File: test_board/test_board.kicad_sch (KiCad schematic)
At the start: 14 parts, among them J1 Conn_01x24_Socket, J2 Conn_01x24_Socket, SW1 CJS-1201B, U14 REF3012, U15 REF3025, U4 HT7533-1_C14289

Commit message: added uart connector
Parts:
- added J3: Conn_01x02_Pin, Connector_PinHeader_2.54mm:PinHeader_1x02_P2.54mm_Vertical, symbol Connector:Conn_01x02_Pin
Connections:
- net pin22: now reaches J1.22 (Pin_22)
- net pin22: now also J3.1 (Pin_1)
- net pin23: now reaches J1.23 (Pin_23)
- net pin23: now also J3.2 (Pin_2)
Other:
- note added: "5V current budget: Per datasheet FPGA worst case power consumption: 1.2A @ 1V 0.6A @ 1.8V 0.6A @ 3.3V 4.26 W total 0.0625 @ 5V from comparators 4.57 W 915 mA, USB 3.0 ports max out at 900mA, 2.0 maxes out at 500mA If we have problems we use an external 5V/2A USB supply then communicate to pc over a broken out UART interface"
- note added: "Extra pins broken out in case we need an additional comms interface"
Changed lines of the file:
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@@
 		)
 	)
+	(text "5V current budget:\nPer datasheet FPGA worst case power consumption:\n1.2A @ 1V \n0.6A @ 1.8V\n0.6A @ 3.3V\n4.26 W total\n0.0625 @ 5V from comparators\n4.57 W\n915 mA, USB 3.0 ports max out at 900mA, 2.0 maxes out at 500mA\nIf we have problems we use an external 5V/2A USB supply\nthen communicate to pc over a broken out UART interface"
+		(exclude_from_sim no)
+		(at 15.24 173.355 0)
+		(effects
+			(font
+				(size 1.27 1.27)
+			)
+			(justify left)
+		)
+	)
 	(text "3.3V current budget:\nComparators: 5.8 mA * 10 = 58 mA\nVoltage reference dividers: 700uA * 10 = 7mA\nVoltage reference quiescent: 25uA * 10 = 250uA\nTotal: 65.25 mA"
 		(exclude_from_sim no)
-		(at 26.67 152.4 0)
+		(at 15.24 153.035 0)
+		(effects
+			(font
+				(size 1.27 1.27)
+			)
+			(justify left)
+		)
+	)
+	(text "Extra pins broken out in case we\nneed an additional comms interface"
+		(exclude_from_sim no)
+		(at 42.545 191.135 0)
 		(effects
 			(font
@@
 		)
 	)
+	(global_label "pin22"
+		(shape bidirectional)
+		(at 95.25 170.18 180)
+		(fields_autoplaced yes)
+		(effects
+			(font
+				(size 1.27 1.27)
+			)
+			(justify right)
+		)
+		(property "Intersheetrefs" "${INTERSHEET_REFS}"
+			(at 85.8317 170.18 0)
+			(effects
+				(font
+					(size 1.27 1.27)
+				)
+				(justify right)
+				(hide yes)
+			)
+		)
+	)
+	(global_label "pin23"
+		(shape bidirectional)
+		(at 90.17 192.405 0)
+		(fields_autoplaced yes)
+		(effects
+			(font
+				(size 1.27 1.27)
+			)
+			(justify left)
+		)
+		(property "Intersheetrefs" "${INTERSHEET_REFS}"
+			(at 99.5883 192.405 0)
+			(effects
+				(font
+					(size 1.27 1.27)
+				)
+				(justify left)
+				(hide yes)
+			)
+		)
+	)
 	(global_label "out2"
 		(shape input)
@@
 		)
 	)
+	(global_label "pin23"
+		(shape bidirectional)
+		(at 95.25 172.72 180)
+		(fields_autoplaced yes)
+		(effects
+			(font
+				(size 1.27 1.27)
+			)
+			(justify right)
+		)
+		(property "Intersheetrefs" "${INTERSHEET_REFS}"
+			(at 85.8317 172.72 0)
+			(effects
+				(font
+					(size 1.27 1.27)
+				)
+				(justify right)
+				(hide yes)
+			)
+		)
+	)
+	(global_label "pin22"
+		(shape bidirectional)
+		(at 90.17 189.865 0)
+		(fields_autoplaced yes)
+		(effects
+			(font
+				(size 1.27 1.27)
+			)
+			(justify left)
+		)
+		(property "Intersheetrefs" "${INTERSHEET_REFS}"
+			(at 99.5883 189.865 0)
+			(effects
+				(font
+					(size 1.27 1.27)
+				)
+				(justify left)
+				(hide yes)
+			)
+		)
+	)
 	(global_label "vref"
 		(shape input)
@@
 					(unit 1)
 				)
+			)
+		)
+	)
+	(symbol
+		(lib_id "Connector:Conn_01x02_Pin")
+		(at 85.09 189.865 0)
+		(unit 1)
+		(exclude_from_sim no)
+		(in_bom yes)
+		(on_board yes)
+		(dnp yes)
+		(fields_autoplaced yes)
+		(property "Reference" "J3"
+			(at 85.725 184.785 0)
+			(effects
+				(font
+					(size 1.27 1.27)
+				)
+			)
+		)
+		(property "Value" "Conn_01x02_Pin"
+			(at 85.725 187.325 0)
+			(effects
+				(font
+					(size 1.27 1.27)
+				)
+			)
+		)
+		(property "Footprint" "Connector_PinHeader_2.54mm:PinHeader_1x02_P2.54mm_Vertical"
+			(at 85.09 189.865 0)
+			(effects
+				(font
+					(size 1.27 1.27)
+				)
+				(hide yes)
+			)
+		)
+		(property "Datasheet" "~"
+			(at 85.09 189.865 0)
+			(effects
+				(font
+					(size 1.27 1.27)
+				)
+				(hide yes)
+			)
+		)
+		(property "Description" "Generic connector, single row, 01x02, script generated"
+			(at 85.09 189.865 0)
+			(effects
+				(font
+					(size 1.27 1.27)
+				)
+				(hide yes)
+			)
+		)
+		(pin "1"
+		)
+		(pin "2"
+		)
+		(instances
+			(project ""
+				(path "/f01d8a8e-7bb6-4363-8f3a-aad691292558"
+					(reference "J3")
+					(unit 1)
+				)

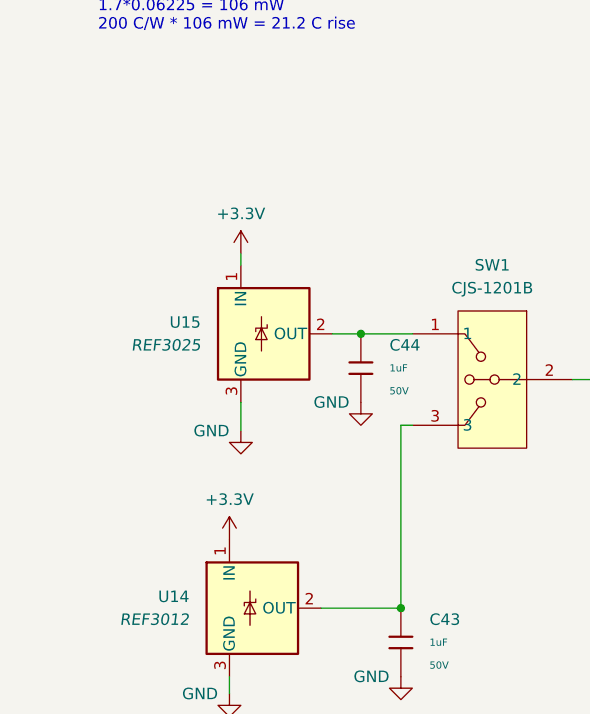
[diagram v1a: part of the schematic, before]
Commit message: added decoupling caps to regulator and changed comparator termination resistor to 49.9 ohm
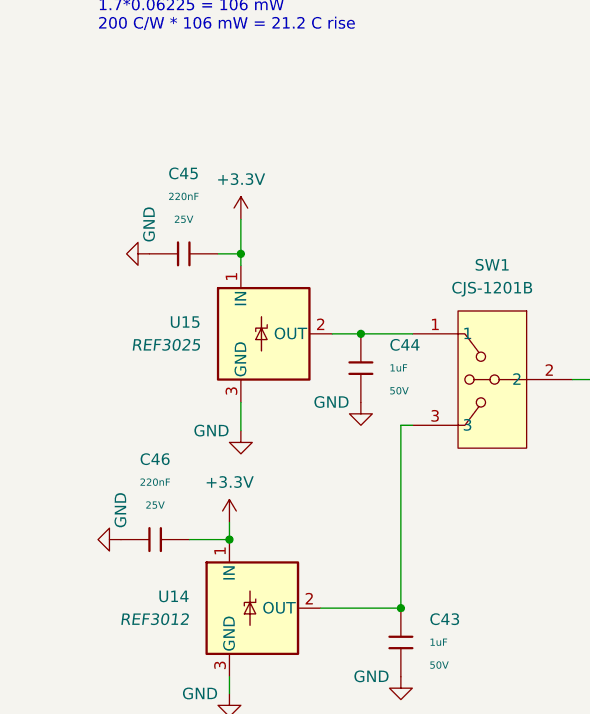
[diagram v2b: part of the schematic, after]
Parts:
- added C45, C46: 220nF, PCM_JLCPCB:C_0603, symbol PCM_JLCPCB-Capacitors:0603,220nF
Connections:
- net +3.3V: now also C45.2, C46.2
- net GND: now also C45.1, C46.1

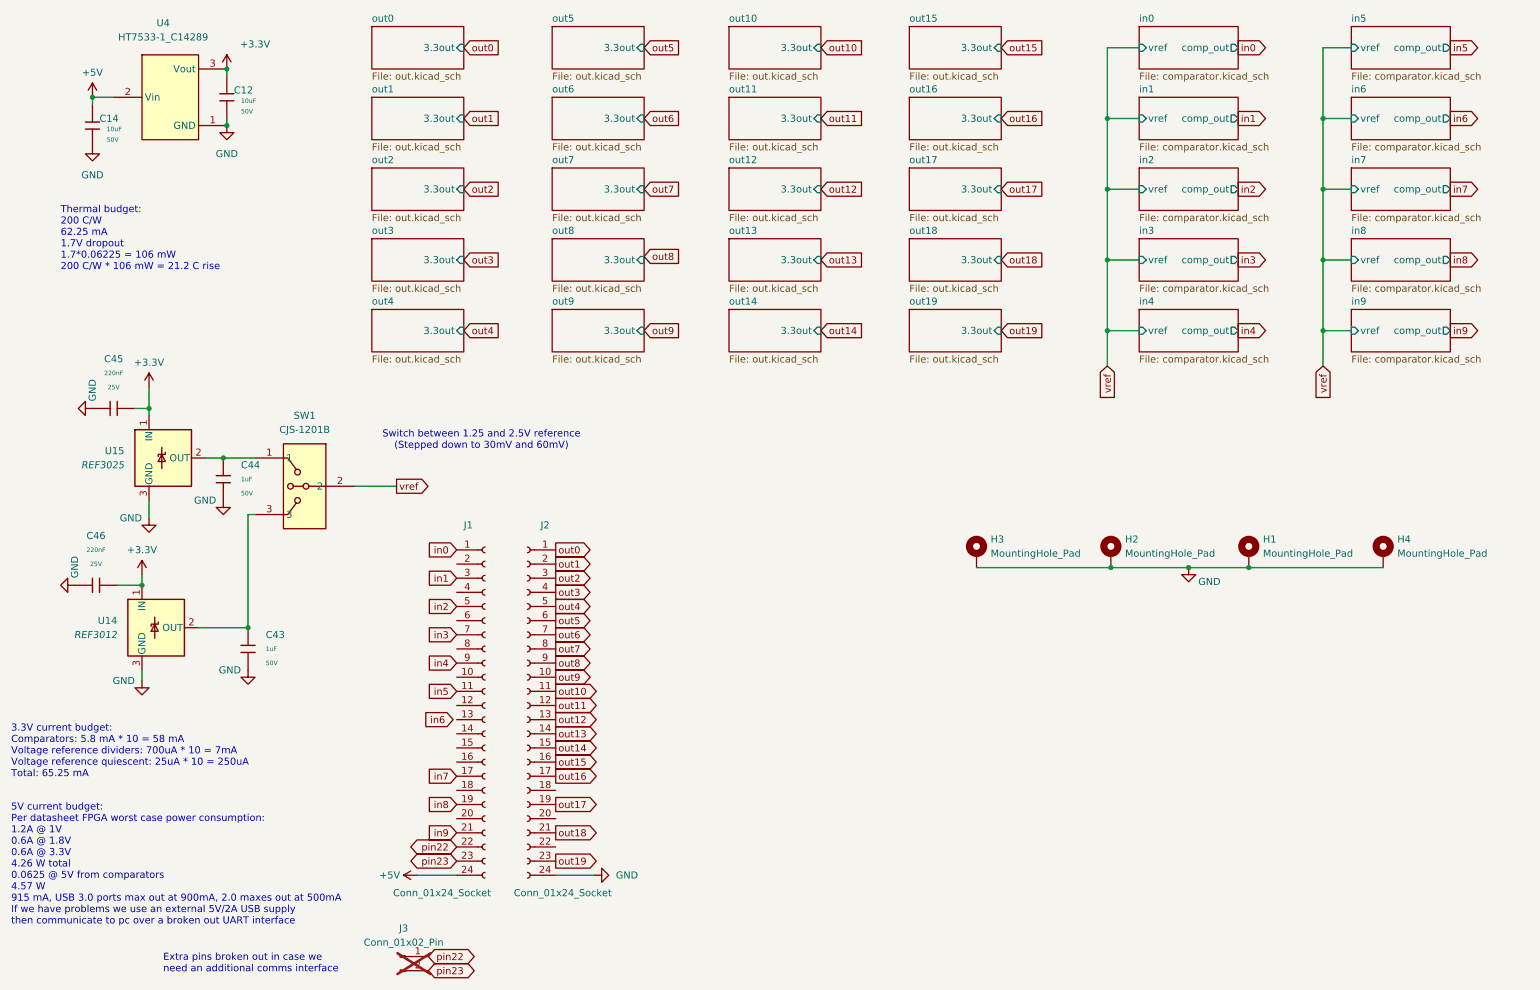
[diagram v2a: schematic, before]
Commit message: spaced out SMA connectors
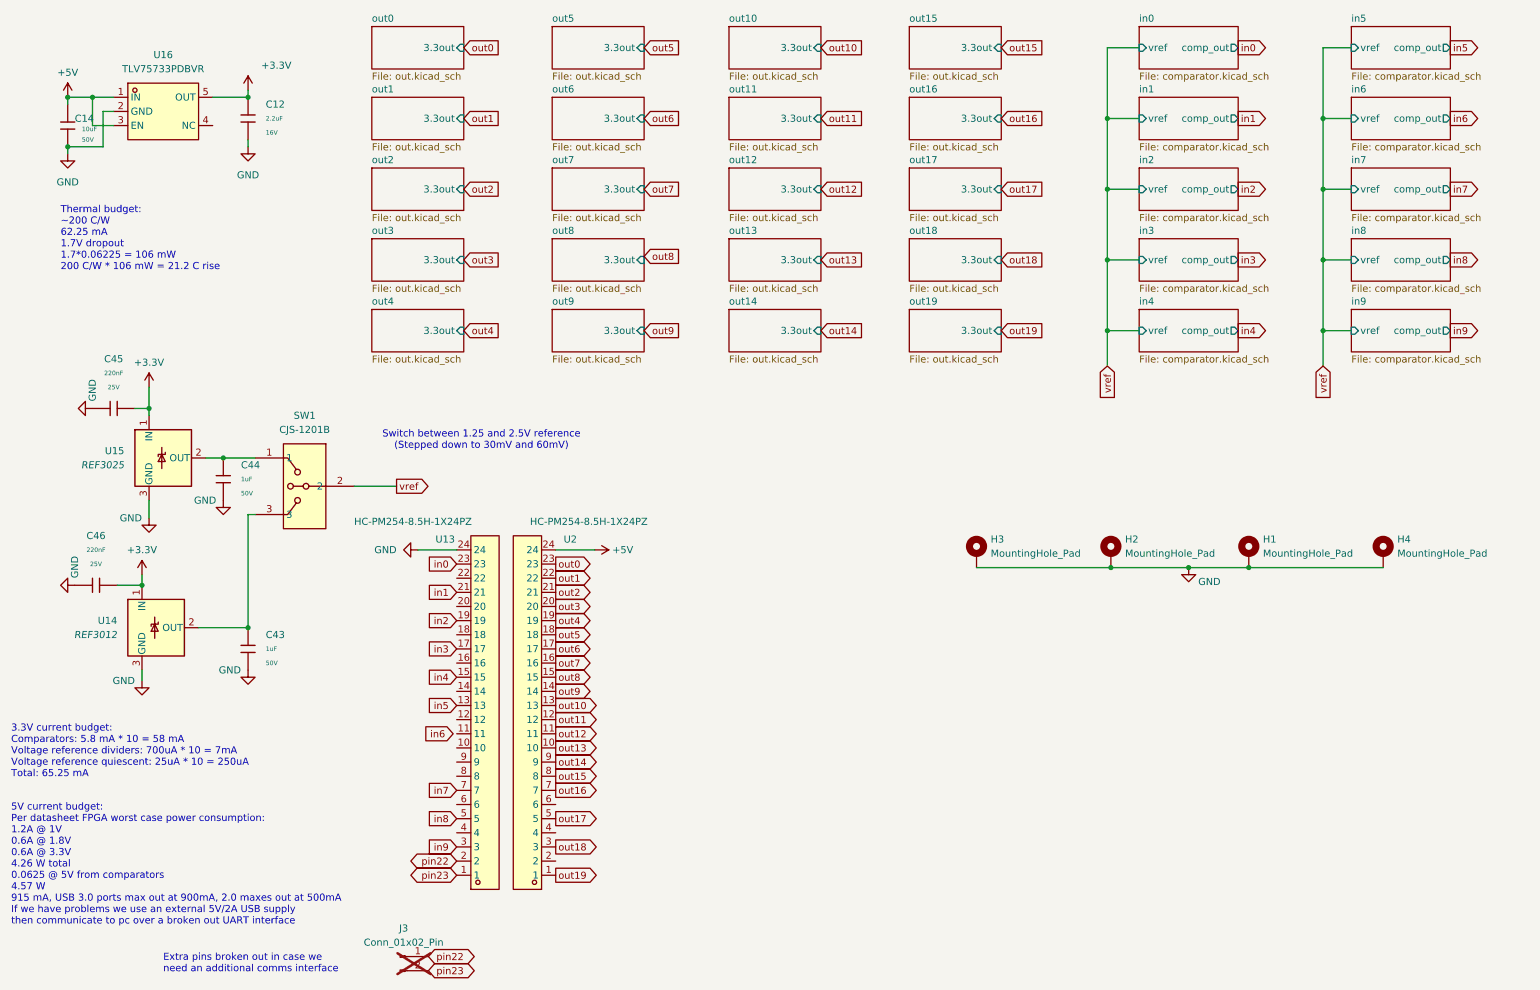
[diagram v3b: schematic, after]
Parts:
- removed C12: 10uF, PCM_JLCPCB:C_0805, symbol PCM_JLCPCB-Capacitors:0805,10uF,(2)
- removed J1, J2: Conn_01x24_Socket, Connector_PinSocket_2.54mm:PinSocket_1x24_P2.54mm_Vertical, symbol Connector:Conn_01x24_Socket
- removed U4: HT7533-1_C14289, easyeda2kicad:SOT-89-3_L4.5-W2.5-P1.50-LS4.2-BR, symbol easyeda2kicad:HT7533-1_C14289
- added C12: 2.2uF, PCM_JLCPCB:C_0603, symbol PCM_JLCPCB-Capacitors:0603,2.2uF
- added U13, U2: HC-PM254-8.5H-1X24PZ, easyeda2kicad:HDR-TH_24P-P2.54-V-F, symbol easyeda2kicad:HC-PM254-8.5H-1X24PZ
- added U16: TLV75733PDBVR, easyeda2kicad:SOT-23-5_L2.9-W1.6-P0.95-LS2.8-BL, symbol easyeda2kicad:TLV75733PDBVR
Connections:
- net +3.3V: now also C12.1, U16.5 (OUT)
- net +5V: now also U16.1 (IN), U16.3 (EN), U2.24
- net GND: now also C12.2, U13.24, U16.2 (GND)
- net in0: now also U13.23
- net in1: now also U13.21
- net in2: now also U13.19
- net in3: now also U13.17
- net in4: now also U13.15
- net in5: now also U13.13
- net in7: now also U13.7
- net in8: now also U13.5
- net in9: now also U13.3
- net out0: now also U2.23
- net out1: now also U2.22
- net out10: now also U2.13
- net out11: now also U2.12
- net out12: now also U2.11
- net out13: now also U2.10
- net out14: now also U2.9
- net out15: now also U2.8
- net out16: now also U2.7
- net out17: now also U2.5
- net out18: now also U2.3
- net out19: now also U2.1
- net out2: now also U2.21
- net out3: now also U2.20
- net out4: now also U2.19
- net out5: now also U2.18
- net out6: now also U2.17
- net out7: now also U2.16
- net out8: now also U2.15
- net out9: now also U2.14
- net pin22: now also U13.2
- net pin23: now also U13.1
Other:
- note added: "Thermal budget: ~200 C/W 62.25 mA 1.7V dropout 1.7*0.06225 = 106 mW 200 C/W * 106 mW = 21.2 C rise"
- note removed: "Thermal budget: 200 C/W 62.25 mA 1.7V dropout 1.7*0.06225 = 106 mW 200 C/W * 106 mW = 21.2 C rise"
- moved on the sheet: C14

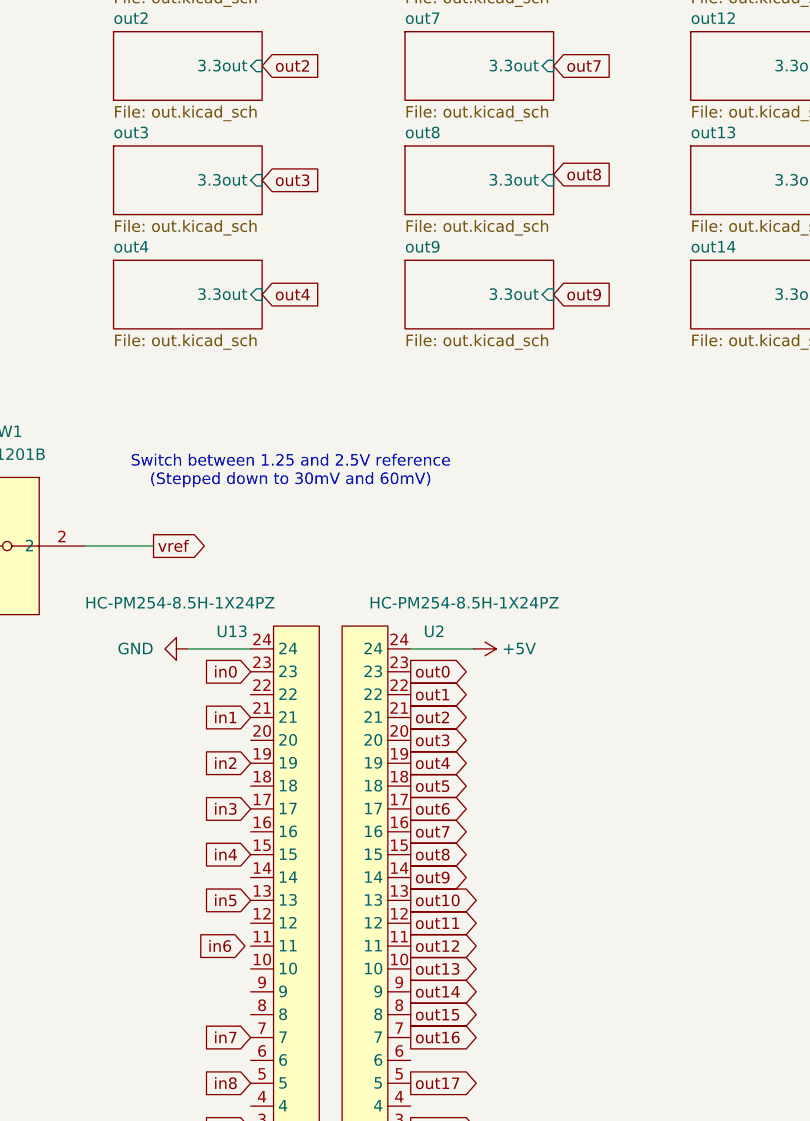
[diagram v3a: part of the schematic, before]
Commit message: finished routing just need to add fencing vias
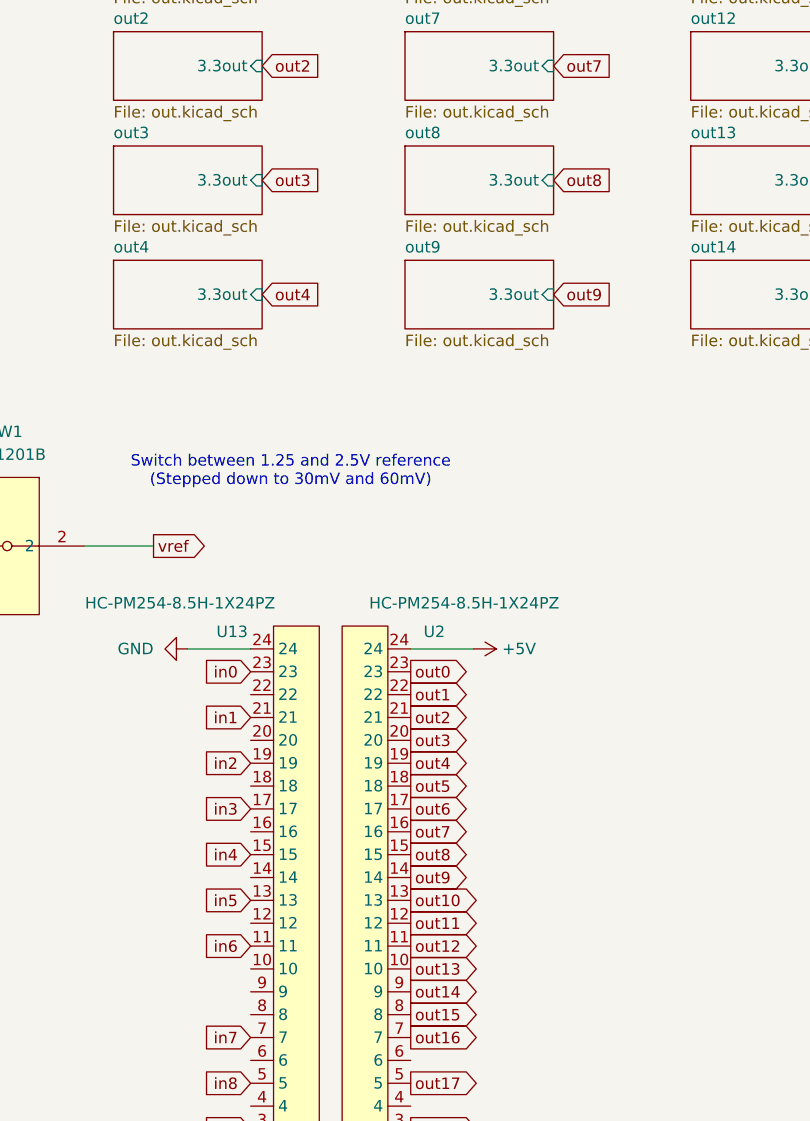
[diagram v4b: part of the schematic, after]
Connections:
- net in6: now also U13.11
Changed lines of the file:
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@@
 	(global_label "in6"
 		(shape input)
-		(at 94.615 149.86 180)
+		(at 95.25 149.86 180)
 		(fields_autoplaced yes)
 		(effects
@@
 		)
 		(property "Intersheetrefs" "${INTERSHEET_REFS}"
-			(at 88.6665 149.86 0)
+			(at 89.3015 149.86 0)
 			(effects
 				(font
@@
 	(global_label "out8"
 		(shape input)
-		(at 128.905 64.135 0)
-		(fields_autoplaced yes)
-		(effects
-			(font
-				(size 1.27 1.27)
-			)
-			(justify left)
-		)
-		(property "Intersheetrefs" "${INTERSHEET_REFS}"
-			(at 136.1234 64.135 0)
-			(effects
-				(font
+		(at 128.905 64.77 0)
+		(fields_autoplaced yes)
+		(effects
+			(font
+				(size 1.27 1.27)
+			)
+			(justify left)
+		)
+		(property "Intersheetrefs" "${INTERSHEET_REFS}"
+			(at 136.1234 64.77 0)
+			(effects
+				(font

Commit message: finished board
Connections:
- net out10: now also U2.11; no longer U2.13
- net out11: now also U2.10; no longer U2.12
- net out12: now also U2.9; no longer U2.11
- net out13: now also U2.8; no longer U2.10
- net out14: now also U2.7; no longer U2.9
- net out15: now also U2.6; no longer U2.8
- net out16: now also U2.5; no longer U2.7
- net out17: now also U2.4; no longer U2.5
- net out7: now also U2.14; no longer U2.16
- net out8: now also U2.13; no longer U2.15
- net out9: now also U2.12; no longer U2.14
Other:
- note added: "50-ohm traces designed for JLC0416H-7628 stackup 0.035mm copper 0.21040mm prepreg 0.0152mm copper 0.31mm trace width 0.132mm clearence Coplanar wave guide w/ ground plane 49.95 Ohm"
